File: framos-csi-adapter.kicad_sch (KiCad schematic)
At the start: 68 parts, among them J1 Conn_Hirose_DF40C-60DS-0.4V51, J2 Conn_STM_MSAK24025P30, U1 NTS0102_XSON, U2 AP62301Z6-7, U3 AP62301Z6-7

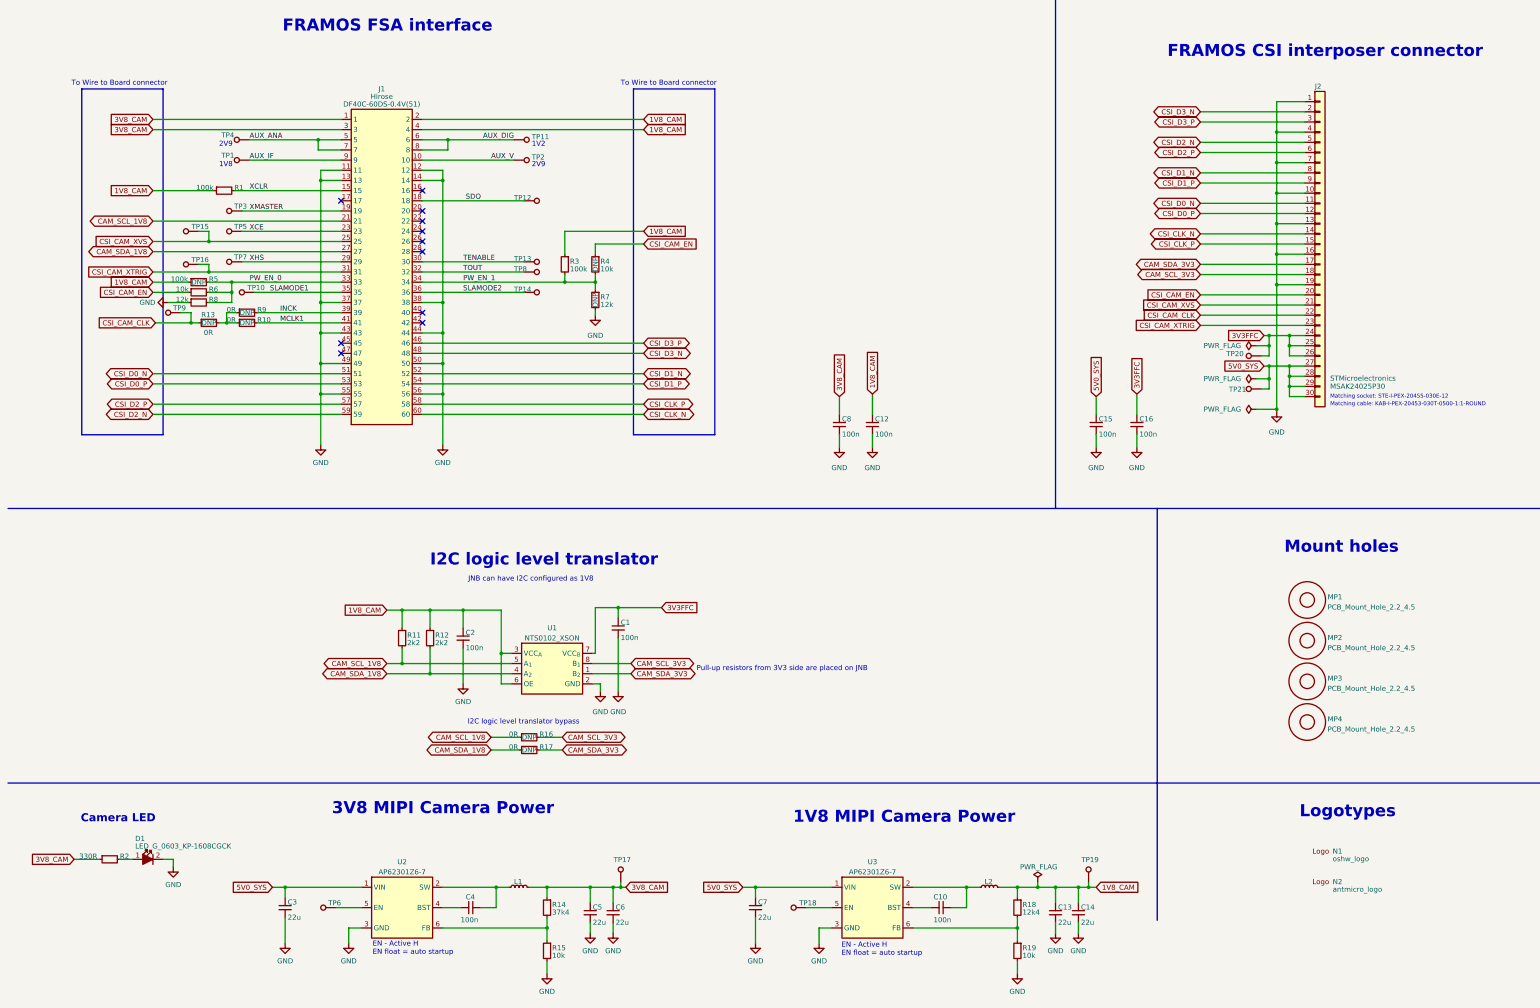
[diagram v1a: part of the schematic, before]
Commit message: [#56796] Fix lib references
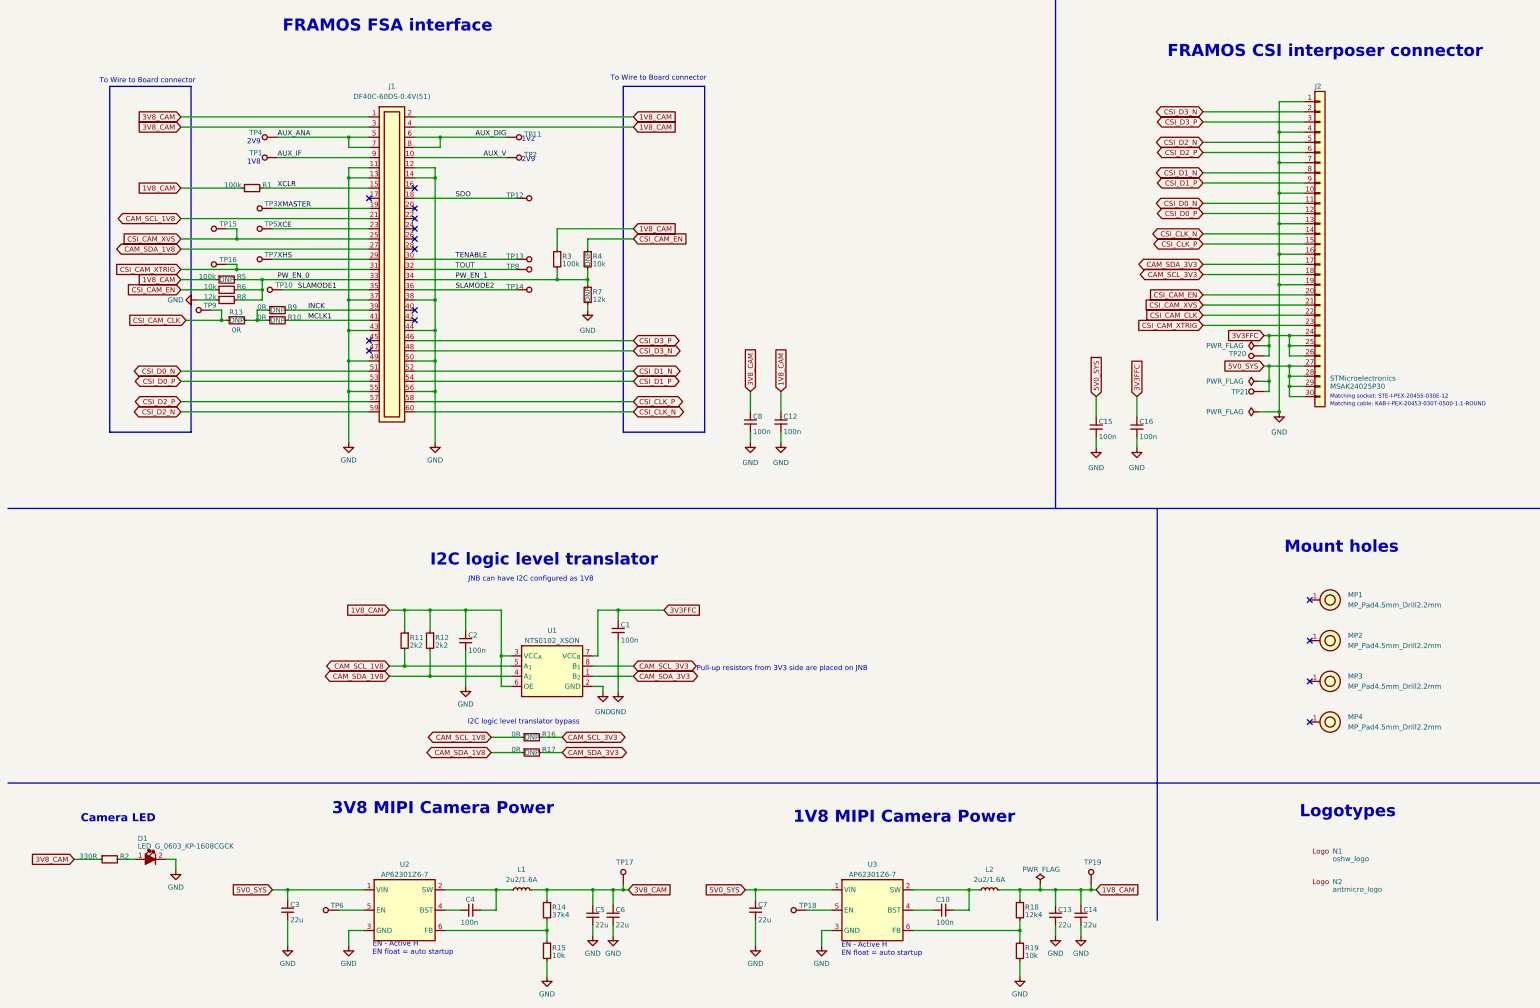
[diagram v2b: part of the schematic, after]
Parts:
- C1, C10, C12, C15, C16, C2, C4, C8: footprint framos-csi-adapter-footprints:C_0402_1005Metric -> antmicro-footprints:C_0402_1005Metric; symbol framos-csi-adapter:C_100n_0402 -> antmicroCapacitors0402:C_100n_0402
- C13, C14, C3, C5, C6, C7: footprint framos-csi-adapter-footprints:C_0603_1608Metric -> antmicro-footprints:C_0603_1608Metric; symbol framos-csi-adapter:C_22u_0603 -> antmicroCapacitors0603:C_22u_0603
- D1: footprint framos-csi-adapter-footprints:LED_0603_1608Metric_G -> antmicro-footprints:LED_0603_1608Metric_G; symbol framos-csi-adapter:LED_G_0603_KP-1608CGCK -> antmicroLEDIndicationDiscrete:LED_G_0603_KP-1608CGCK
- J1: value Conn_Hirose_DF40C-60DS-0.4V51 -> Socket_Hirose_DF40_2x30_DF40C-60DS-0.4V; footprint framos-csi-adapter-footprints:Conn_Hirose_DF40C-60DS-0.4V51 -> antmicro-footprints:Conn_Socket_Hirose_DF40_2x30_DF40C-60DS-0.4V; symbol framos-csi-adapter:Conn_Hirose_DF40C-60DS-0.4V51 -> antmicroB2BConnectors:Socket_Hirose_DF40_2x30_DF40C-60DS-0.4V; Manufacturer Hirose -> Hirose Electric; Pitch (none) -> 0.4 mm
- J2: footprint framos-csi-adapter-footprints:Conn_STM_MSAK24025P30 -> antmicro-footprints:Conn_STM_MSAK24025P30; symbol framos-csi-adapter:Conn_STM_MSAK24025P30 -> antmicroFCCConnectors:Conn_STM_MSAK24025P30
- L1, L2: value 74479887222C -> L_2u2_1.6A_1008; footprint framos-csi-adapter-footprints:L_1008_2520Metric -> antmicro-footprints:L_1008_2520Metric; symbol framos-csi-adapter:74479887222C -> antmicroFixedInductors:L_2u2_1.6A_1008; IMax (none) -> 1.6 A; ISat (none) -> 1.5 A; Val (none) -> 2u2/1.6A
- MP1, MP2, MP3, MP4: value PCB_Mount_Hole_2.2_4.5 -> MP_Pad4.5mm_Drill2.2mm; footprint framos-csi-adapter-footprints:mounting-hole-2.2mm -> antmicro-footprints:MP_Pad4.5mm_Drill2.2mm; symbol framos-csi-adapter:PCB_Mount_Hole_2.2_4.5 -> antmicroMechanicalParts:MP_Pad4.5mm_Drill2.2mm; now left out of the parts list
- N1: footprint framos-csi-adapter-footprints:OSHW-Logo2_7.3x6mm_Copper_Mask -> antmicro-footprints:oshw-logo; symbol framos-csi-adapter:oshw_logo -> antmicroMechanicalParts:oshw_logo
- N2: footprint framos-csi-adapter-footprints:antmicro-logo_scaled_12mm -> antmicro-footprints:antmicro-logo; symbol framos-csi-adapter:antmicro_logo -> antmicroMechanicalParts:antmicro_logo
- R1, R3, R5: footprint framos-csi-adapter-footprints:R_0402_1005Metric -> antmicro-footprints:R_0402_1005Metric; symbol framos-csi-adapter:R_100k_0402 -> antmicroResistors0402:R_100k_0402
- R10, R13, R16, R17, R9: footprint framos-csi-adapter-footprints:R_0402_1005Metric -> antmicro-footprints:R_0402_1005Metric; symbol framos-csi-adapter:R_0R_0402 -> antmicroResistors0402:R_0R_0402
- R11, R12: footprint framos-csi-adapter-footprints:R_0402_1005Metric -> antmicro-footprints:R_0402_1005Metric; symbol framos-csi-adapter:R_2k2_0402 -> antmicroResistors0402:R_2k2_0402
- R14: footprint framos-csi-adapter-footprints:R_0402_1005Metric -> antmicro-footprints:R_0402_1005Metric; symbol framos-csi-adapter:R_37k4_0402 -> antmicroResistors0402:R_37k4_0402
- R15, R19, R4, R6: footprint framos-csi-adapter-footprints:R_0402_1005Metric -> antmicro-footprints:R_0402_1005Metric; symbol framos-csi-adapter:R_10k_0402 -> antmicroResistors0402:R_10k_0402
- R18: footprint framos-csi-adapter-footprints:R_0402_1005Metric -> antmicro-footprints:R_0402_1005Metric; symbol framos-csi-adapter:R_12k4_0402 -> antmicroResistors0402:R_12k4_0402
- R2: footprint framos-csi-adapter-footprints:R_0402_1005Metric -> antmicro-footprints:R_0402_1005Metric; symbol framos-csi-adapter:R_330R_0402 -> antmicroResistors0402:R_330R_0402
- R7, R8: footprint framos-csi-adapter-footprints:R_0402_1005Metric -> antmicro-footprints:R_0402_1005Metric; symbol framos-csi-adapter:R_12k_0402 -> antmicroResistors0402:R_12k_0402
- TP1, TP10, TP11, TP12, TP13, TP14, TP15, TP16, TP17, TP19, TP2, TP20, TP21, TP3, TP4, TP5, TP6, TP7, TP8, TP9: footprint framos-csi-adapter-footprints:TP_SMD_0.75mm -> antmicro-footprints:TP_SMD_0.75mm; symbol framos-csi-adapter:TP_0.75mm_SMD -> antmicroTestPoints:TP_0.75mm_SMD
- TP18: footprint framos-csi-adapter-footprints:Testpoint_smd_1mm -> antmicro-footprints:TP_SMD_1mm; symbol framos-csi-adapter:TP_1mm_SMD -> antmicroTestPoints:TP_1mm_SMD
- U1: footprint framos-csi-adapter-footprints:XSON-8_1x1.95mm_P0.5mm -> antmicro-footprints:XSON-8_1x1.95mm_P0.5mm; symbol framos-csi-adapter:NTS0102_XSON -> antmicroLogicTranslatorsLevelShifters:NTS0102_XSON
- U2, U3: footprint framos-csi-adapter-footprints:SOT-563 -> antmicro-footprints:SOT-563; symbol framos-csi-adapter:AP62301Z6-7 -> antmicroDCDCConverters:AP62301Z6-7
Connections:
- no-connect marks 11 -> 15
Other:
- moved on the sheet: C1, C10, C12, C13, C14, C15, C16, C2, C3, C4, C5, C6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

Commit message: [#56796] Loclib
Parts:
- C1, C10, C12, C15, C16, C2, C4, C8: footprint antmicro-footprints:C_0402_1005Metric -> framos-csi-adapter-footprints:C_0402_1005Metric; symbol antmicroCapacitors0402:C_100n_0402 -> framos-csi-adapter:C_100n_0402
- C13, C14, C3, C5, C6, C7: footprint antmicro-footprints:C_0603_1608Metric -> framos-csi-adapter-footprints:C_0603_1608Metric; symbol antmicroCapacitors0603:C_22u_0603 -> framos-csi-adapter:C_22u_0603
- D1: footprint antmicro-footprints:LED_0603_1608Metric_G -> framos-csi-adapter-footprints:LED_0603_1608Metric_G; symbol antmicroLEDIndicationDiscrete:LED_G_0603_KP-1608CGCK -> framos-csi-adapter:LED_G_0603_KP-1608CGCK
- J1: footprint antmicro-footprints:Conn_Socket_Hirose_DF40_2x30_DF40C-60DS-0.4V -> framos-csi-adapter-footprints:Conn_Socket_Hirose_DF40_2x30_DF40C-60DS-0.4V; symbol antmicroB2BConnectors:Socket_Hirose_DF40_2x30_DF40C-60DS-0.4V -> framos-csi-adapter:Socket_Hirose_DF40_2x30_DF40C-60DS-0.4V
- J2: footprint antmicro-footprints:Conn_STM_MSAK24025P30 -> framos-csi-adapter-footprints:Conn_STM_MSAK24025P30; symbol antmicroFCCConnectors:Conn_STM_MSAK24025P30 -> framos-csi-adapter:Conn_STM_MSAK24025P30
- L1, L2: footprint antmicro-footprints:L_1008_2520Metric -> framos-csi-adapter-footprints:L_1008_2520Metric; symbol antmicroFixedInductors:L_2u2_1.6A_1008 -> framos-csi-adapter:L_2u2_1.6A_1008
- MP1, MP2, MP3, MP4: footprint antmicro-footprints:MP_Pad4.5mm_Drill2.2mm -> framos-csi-adapter-footprints:MP_Pad4.5mm_Drill2.2mm; symbol antmicroMechanicalParts:MP_Pad4.5mm_Drill2.2mm -> framos-csi-adapter:MP_Pad4.5mm_Drill2.2mm
- N1: footprint antmicro-footprints:oshw-logo -> framos-csi-adapter-footprints:oshw-logo; symbol antmicroMechanicalParts:oshw_logo -> framos-csi-adapter:oshw_logo
- N2: footprint antmicro-footprints:antmicro-logo -> framos-csi-adapter-footprints:antmicro-logo; symbol antmicroMechanicalParts:antmicro_logo -> framos-csi-adapter:antmicro_logo
- R1, R3, R5: footprint antmicro-footprints:R_0402_1005Metric -> framos-csi-adapter-footprints:R_0402_1005Metric; symbol antmicroResistors0402:R_100k_0402 -> framos-csi-adapter:R_100k_0402
- R10, R13, R16, R17, R9: footprint antmicro-footprints:R_0402_1005Metric -> framos-csi-adapter-footprints:R_0402_1005Metric; symbol antmicroResistors0402:R_0R_0402 -> framos-csi-adapter:R_0R_0402
- R11, R12: footprint antmicro-footprints:R_0402_1005Metric -> framos-csi-adapter-footprints:R_0402_1005Metric; symbol antmicroResistors0402:R_2k2_0402 -> framos-csi-adapter:R_2k2_0402
- R14: footprint antmicro-footprints:R_0402_1005Metric -> framos-csi-adapter-footprints:R_0402_1005Metric; symbol antmicroResistors0402:R_37k4_0402 -> framos-csi-adapter:R_37k4_0402
- R15, R19, R4, R6: footprint antmicro-footprints:R_0402_1005Metric -> framos-csi-adapter-footprints:R_0402_1005Metric; symbol antmicroResistors0402:R_10k_0402 -> framos-csi-adapter:R_10k_0402
- R18: footprint antmicro-footprints:R_0402_1005Metric -> framos-csi-adapter-footprints:R_0402_1005Metric; symbol antmicroResistors0402:R_12k4_0402 -> framos-csi-adapter:R_12k4_0402
- R2: footprint antmicro-footprints:R_0402_1005Metric -> framos-csi-adapter-footprints:R_0402_1005Metric; symbol antmicroResistors0402:R_330R_0402 -> framos-csi-adapter:R_330R_0402
- R7, R8: footprint antmicro-footprints:R_0402_1005Metric -> framos-csi-adapter-footprints:R_0402_1005Metric; symbol antmicroResistors0402:R_12k_0402 -> framos-csi-adapter:R_12k_0402
- TP1, TP10, TP11, TP12, TP13, TP14, TP15, TP16, TP17, TP19, TP2, TP20, TP21, TP3, TP4, TP5, TP6, TP7, TP8, TP9: footprint antmicro-footprints:TP_SMD_0.75mm -> framos-csi-adapter-footprints:TP_SMD_0.75mm; symbol antmicroTestPoints:TP_0.75mm_SMD -> framos-csi-adapter:TP_0.75mm_SMD
- TP18: symbol antmicroTestPoints:TP_1mm_SMD -> framos-csi-adapter:TP_1mm_SMD
- U1: footprint antmicro-footprints:XSON-8_1x1.95mm_P0.5mm -> framos-csi-adapter-footprints:XSON-8_1x1.95mm_P0.5mm; symbol antmicroLogicTranslatorsLevelShifters:NTS0102_XSON -> framos-csi-adapter:NTS0102_XSON
- U2, U3: footprint antmicro-footprints:SOT-563 -> framos-csi-adapter-footprints:SOT-563; symbol antmicroDCDCConverters:AP62301Z6-7 -> framos-csi-adapter:AP62301Z6-7

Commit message: [#56796] Small PCB fixes, DNP marking
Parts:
- removed N1: oshw_logo, framos-csi-adapter-footprints:oshw-logo, symbol framos-csi-adapter:oshw_logo
- removed N2: antmicro_logo, framos-csi-adapter-footprints:antmicro-logo, symbol framos-csi-adapter:antmicro_logo
- R10, R13, R16, R17, R4, R5, R7, R9: now not fitted; now left out of the parts list
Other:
- note removed: "Logotypes"
- moved on the sheet: MP1, MP2, MP3, MP4
